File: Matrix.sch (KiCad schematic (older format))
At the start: 31 parts

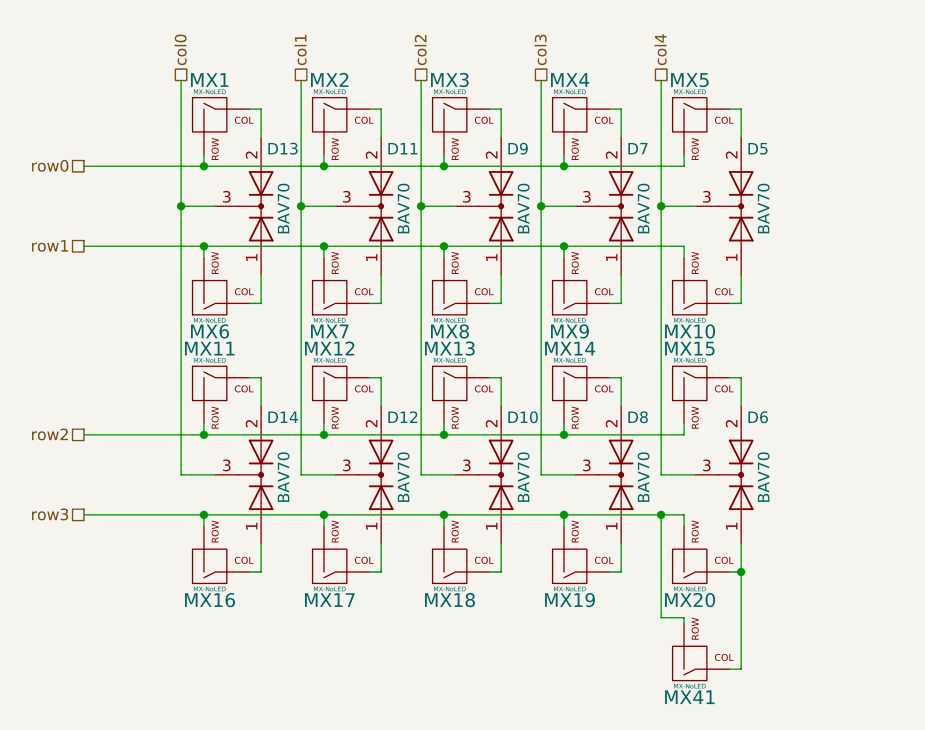
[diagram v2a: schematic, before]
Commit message: Finished right-side, added BOM
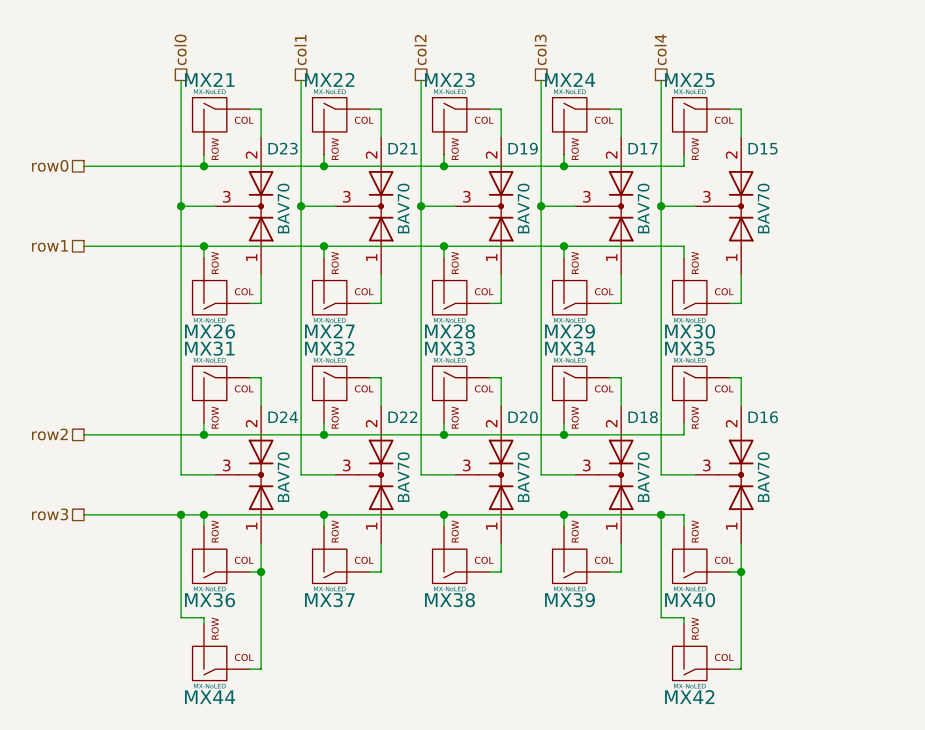
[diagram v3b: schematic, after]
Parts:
- added MX43: MX-NoLED, Ai03-MX:MXOnly-2U-Hotswap, symbol Ai03:MX-NoLED
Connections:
- net row3: now also MX43.2 (ROW)
- net at D14.1 (A), MX16.1 (COL): now also MX43.1 (COL)
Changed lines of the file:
@@
 $Descr A4 11693 8268
 encoding utf-8
-Sheet 4 5
+Sheet 5 5
 Title ""
 Date ""
@@
 AR Path="/5E0FF211/5DC40EE0" Ref="MX?"  Part="1"
 AR Path="/5E103021/5DC40EE0" Ref="MX21"  Part="1"
-F 0 "MX1" H 4725 2975 60  0000 C CNN
+F 0 "MX21" H 4725 2975 60  0000 C CNN
 F 1 "MX-NoLED" H 4725 2925 20  0000 C CNN
 F 2 "Ai03-MX:MXOnly-1U-Hotswap" H 4125 2775 60  0001 C CNN
@@
 AR Path="/5E0FF211/5DC40EF4" Ref="MX?"  Part="1"
 AR Path="/5E103021/5DC40EF4" Ref="MX26"  Part="1"
-F 0 "MX6" H 4725 3725 60  0000 C CNN
+F 0 "MX26" H 4725 3725 60  0000 C CNN
 F 1 "MX-NoLED" H 4725 3675 20  0000 C CNN
 F 2 "Ai03-MX:MXOnly-1U-Hotswap" H 4125 3525 60  0001 C CNN
@@
 AR Path="/5E0FF211/5DC4E718" Ref="MX?"  Part="1"
 AR Path="/5E103021/5DC4E718" Ref="MX31"  Part="1"
-F 0 "MX11" H 4725 4150 60  0000 C CNN
+F 0 "MX31" H 4725 4150 60  0000 C CNN
 F 1 "MX-NoLED" H 4725 4100 20  0000 C CNN
 F 2 "Ai03-MX:MXOnly-1U-Hotswap" H 4125 3950 60  0001 C CNN
@@
 AR Path="/5E0FF211/5DC4E722" Ref="D?"  Part="1"
 AR Path="/5E103021/5DC4E722" Ref="D20"  Part="1"
-F 0 "D10" V 6250 4375 50  0000 L CNN
+F 0 "D20" V 6250 4375 50  0000 L CNN
 F 1 "BAV70" H 5875 4450 50  0000 L CNN
 F 2 "Package_TO_SOT_SMD:SOT-23_Handsoldering" H 6000 4350 50  0001 C CNN
@@
 AR Path="/5E0FF211/5DC4E731" Ref="MX?"  Part="1"
 AR Path="/5E103021/5DC4E731" Ref="MX36"  Part="1"
-F 0 "MX16" H 4725 4900 60  0000 C CNN
+F 0 "MX36" H 4725 4900 60  0000 C CNN
 F 1 "MX-NoLED" H 4725 4850 20  0000 C CNN
 F 2 "Ai03-MX:MXOnly-1U-Hotswap" H 4125 4700 60  0001 C CNN
@@
 AR Path="/5E0FF211/5DC54A92" Ref="MX?"  Part="1"
 AR Path="/5E103021/5DC54A92" Ref="MX22"  Part="1"
-F 0 "MX2" H 5250 2975 60  0000 C CNN
+F 0 "MX22" H 5250 2975 60  0000 C CNN
 F 1 "MX-NoLED" H 5250 2925 20  0000 C CNN
 F 2 "Ai03-MX:MXOnly-1U-Hotswap" H 4650 2775 60  0001 C CNN
@@
 AR Path="/5E0FF211/5DC54AAB" Ref="MX?"  Part="1"
 AR Path="/5E103021/5DC54AAB" Ref="MX27"  Part="1"
-F 0 "MX7" H 5250 3725 60  0000 C CNN
+F 0 "MX27" H 5250 3725 60  0000 C CNN
 F 1 "MX-NoLED" H 5250 3675 20  0000 C CNN
 F 2 "Ai03-MX:MXOnly-1U-Hotswap" H 4650 3525 60  0001 C CNN
@@
 AR Path="/5E0FF211/5DC54AB7" Ref="MX?"  Part="1"
 AR Path="/5E103021/5DC54AB7" Ref="MX32"  Part="1"
-F 0 "MX12" H 5250 4150 60  0000 C CNN
+F 0 "MX32" H 5250 4150 60  0000 C CNN
 F 1 "MX-NoLED" H 5250 4100 20  0000 C CNN
 F 2 "Ai03-MX:MXOnly-1U-Hotswap" H 4650 3950 60  0001 C CNN
@@
 AR Path="/5E0FF211/5DC54AC1" Ref="D?"  Part="1"
 AR Path="/5E103021/5DC54AC1" Ref="D21"  Part="1"
-F 0 "D11" V 5725 3200 50  0000 L CNN
+F 0 "D21" V 5725 3200 50  0000 L CNN
 F 1 "BAV70" H 5350 3275 50  0000 L CNN
 F 2 "Package_TO_SOT_SMD:SOT-23_Handsoldering" H 5475 3175 50  0001 C CNN
@@
 AR Path="/5E0FF211/5DC54AD0" Ref="MX?"  Part="1"
 AR Path="/5E103021/5DC54AD0" Ref="MX37"  Part="1"
-F 0 "MX17" H 5250 4900 60  0000 C CNN
+F 0 "MX37" H 5250 4900 60  0000 C CNN
 F 1 "MX-NoLED" H 5250 4850 20  0000 C CNN
 F 2 "Ai03-MX:MXOnly-1U-Hotswap" H 4650 4700 60  0001 C CNN
@@
 Connection ~ 4700 3000
 Wire Wire Line
-	4700 4525 4175 4525
+	4700 4525 4600 4525
 Wire Wire Line
 	4700 4175 4175 4175
@@
 AR Path="/5E0FF211/5DC60A2A" Ref="MX?"  Part="1"
 AR Path="/5E103021/5DC60A2A" Ref="MX23"  Part="1"
-F 0 "MX3" H 5775 2975 60  0000 C CNN
+F 0 "MX23" H 5775 2975 60  0000 C CNN
 F 1 "MX-NoLED" H 5775 2925 20  0000 C CNN
 F 2 "Ai03-MX:MXOnly-1U-Hotswap" H 5175 2775 60  0001 C CNN
@@
 AR Path="/5E0FF211/5DC60A43" Ref="MX?"  Part="1"
 AR Path="/5E103021/5DC60A43" Ref="MX28"  Part="1"
-F 0 "MX8" H 5775 3725 60  0000 C CNN
+F 0 "MX28" H 5775 3725 60  0000 C CNN
 F 1 "MX-NoLED" H 5775 3675 20  0000 C CNN
 F 2 "Ai03-MX:MXOnly-1U-Hotswap" H 5175 3525 60  0001 C CNN
@@
 AR Path="/5E0FF211/5DC60A4F" Ref="MX?"  Part="1"
 AR Path="/5E103021/5DC60A4F" Ref="MX33"  Part="1"
-F 0 "MX13" H 5775 4150 60  0000 C CNN
+F 0 "MX33" H 5775 4150 60  0000 C CNN
 F 1 "MX-NoLED" H 5775 4100 20  0000 C CNN
 F 2 "Ai03-MX:MXOnly-1U-Hotswap" H 5175 3950 60  0001 C CNN
@@
 AR Path="/5E0FF211/5DC60A59" Ref="D?"  Part="1"
 AR Path="/5E103021/5DC60A59" Ref="D22"  Part="1"
-F 0 "D12" V 5725 4375 50  0000 L CNN
+F 0 "D22" V 5725 4375 50  0000 L CNN
 F 1 "BAV70" H 5350 4450 50  0000 L CNN
 F 2 "Package_TO_SOT_SMD:SOT-23_Handsoldering" H 5475 4350 50  0001 C CNN
@@
 AR Path="/5E0FF211/5DC60A68" Ref="MX?"  Part="1"
 AR Path="/5E103021/5DC60A68" Ref="MX38"  Part="1"
-F 0 "MX18" H 5775 4900 60  0000 C CNN
+F 0 "MX38" H 5775 4900 60  0000 C CNN
 F 1 "MX-NoLED" H 5775 4850 20  0000 C CNN
 F 2 "Ai03-MX:MXOnly-1U-Hotswap" H 5175 4700 60  0001 C CNN
@@
 AR Path="/5E0FF211/5DC60A77" Ref="MX?"  Part="1"
 AR Path="/5E103021/5DC60A77" Ref="MX24"  Part="1"
-F 0 "MX4" H 6300 2975 60  0000 C CNN
+F 0 "MX24" H 6300 2975 60  0000 C CNN
 F 1 "MX-NoLED" H 6300 2925 20  0000 C CNN
 F 2 "Ai03-MX:MXOnly-1U-Hotswap" H 5700 2775 60  0001 C CNN
@@
 AR Path="/5E0FF211/5DC60A90" Ref="MX?"  Part="1"
 AR Path="/5E103021/5DC60A90" Ref="MX29"  Part="1"
-F 0 "MX9" H 6300 3725 60  0000 C CNN
+F 0 "MX29" H 6300 3725 60  0000 C CNN
 F 1 "MX-NoLED" H 6300 3675 20  0000 C CNN
 F 2 "Ai03-MX:MXOnly-1U-Hotswap" H 5700 3525 60  0001 C CNN
@@
 AR Path="/5E0FF211/5DC60A9C" Ref="MX?"  Part="1"
 AR Path="/5E103021/5DC60A9C" Ref="MX34"  Part="1"
-F 0 "MX14" H 6300 4150 60  0000 C CNN
+F 0 "MX34" H 6300 4150 60  0000 C CNN
 F 1 "MX-NoLED" H 6300 4100 20  0000 C CNN
 F 2 "Ai03-MX:MXOnly-1U-Hotswap" H 5700 3950 60  0001 C CNN
@@
 AR Path="/5E0FF211/5DC60AB5" Ref="MX?"  Part="1"
 AR Path="/5E103021/5DC60AB5" Ref="MX39"  Part="1"
-F 0 "MX19" H 6300 4900 60  0000 C CNN
+F 0 "MX39" H 6300 4900 60  0000 C CNN
 F 1 "MX-NoLED" H 6300 4850 20  0000 C CNN
 F 2 "Ai03-MX:MXOnly-1U-Hotswap" H 5700 4700 60  0001 C CNN
@@
 AR Path="/5E0FF211/5DC6C6BD" Ref="MX?"  Part="1"
 AR Path="/5E103021/5DC6C6BD" Ref="MX25"  Part="1"
-F 0 "MX5" H 6825 2975 60  0000 C CNN
+F 0 "MX25" H 6825 2975 60  0000 C CNN
 F 1 "MX-NoLED" H 6825 2925 20  0000 C CNN
 F 2 "Ai03-MX:MXOnly-1U-Hotswap" H 6225 2775 60  0001 C CNN
@@
 AR Path="/5E0FF211/5DC6C6D6" Ref="MX?"  Part="1"
 AR Path="/5E103021/5DC6C6D6" Ref="MX30"  Part="1"
-F 0 "MX10" H 6825 3725 60  0000 C CNN
+F 0 "MX30" H 6825 3725 60  0000 C CNN
 F 1 "MX-NoLED" H 6825 3675 20  0000 C CNN
 F 2 "Ai03-MX:MXOnly-1U-Hotswap" H 6225 3525 60  0001 C CNN
@@
 AR Path="/5E0FF211/5DC6C6E2" Ref="MX?"  Part="1"
 AR Path="/5E103021/5DC6C6E2" Ref="MX35"  Part="1"
-F 0 "MX15" H 6825 4150 60  0000 C CNN
+F 0 "MX35" H 6825 4150 60  0000 C CNN
 F 1 "MX-NoLED" H 6825 4100 20  0000 C CNN
 F 2 "Ai03-MX:MXOnly-1U-Hotswap" H 6225 3950 60  0001 C CNN
@@
 AR Path="/5E0FF211/5DC6C6FB" Ref="MX?"  Part="1"
 AR Path="/5E103021/5DC6C6FB" Ref="MX40"  Part="1"
-F 0 "MX20" H 6825 4900 60  0000 C CNN
+F 0 "MX40" H 6825 4900 60  0000 C CNN
 F 1 "MX-NoLED" H 6825 4850 20  0000 C CNN
 F 2 "Ai03-MX:MXOnly-1U-Hotswap" H 6225 4700 60  0001 C CNN
@@
 AR Path="/5E0FF211/5E13B872" Ref="MX?"  Part="1"
 AR Path="/5E103021/5E13B872" Ref="MX42"  Part="1"
-F 0 "MX41" H 6825 5325 60  0000 C CNN
+F 0 "MX42" H 6825 5325 60  0000 C CNN
 F 1 "MX-NoLED" H 6825 5275 20  0000 C CNN
 F 2 "Ai03-MX:MXOnly-2U-Hotswap" H 6225 5125 60  0001 C CNN
@@
 AR Path="/5E0FF211/5DC60AA6" Ref="D?"  Part="1"
 AR Path="/5E103021/5DC60AA6" Ref="D23"  Part="1"
-F 0 "D13" V 5200 3200 50  0000 L CNN
+F 0 "D23" V 5200 3200 50  0000 L CNN
 F 1 "BAV70" H 4825 3275 50  0000 L CNN
 F 2 "Package_TO_SOT_SMD:SOT-23_Handsoldering" H 4950 3175 50  0001 C CNN
@@
 AR Path="/5E0FF211/5DC60A34" Ref="D?"  Part="1"
 AR Path="/5E103021/5DC60A34" Ref="D17"  Part="1"
-F 0 "D7" V 6775 3200 50  0000 L CNN
+F 0 "D17" V 6775 3200 50  0000 L CNN
 F 1 "BAV70" H 6400 3275 50  0000 L CNN
 F 2 "Package_TO_SOT_SMD:SOT-23_Handsoldering" H 6525 3175 50  0001 C CNN
@@
 AR Path="/5E0FF211/5DC60A81" Ref="D?"  Part="1"
 AR Path="/5E103021/5DC60A81" Ref="D18"  Part="1"
-F 0 "D8" V 6775 4375 50  0000 L CNN
+F 0 "D18" V 6775 4375 50  0000 L CNN
 F 1 "BAV70" H 6400 4450 50  0000 L CNN
 F 2 "Package_TO_SOT_SMD:SOT-23_Handsoldering" H 6525 4350 50  0001 C CNN
@@
 AR Path="/5E0FF211/5DC6C6EC" Ref="D?"  Part="1"
 AR Path="/5E103021/5DC6C6EC" Ref="D24"  Part="1"
-F 0 "D14" V 5200 4375 50  0000 L CNN
+F 0 "D24" V 5200 4375 50  0000 L CNN
 F 1 "BAV70" H 4825 4450 50  0000 L CNN
 F 2 "Package_TO_SOT_SMD:SOT-23_Handsoldering" H 4950 4350 50  0001 C CNN
@@
 AR Path="/5E0FF211/5DC54A9C" Ref="D?"  Part="1"
 AR Path="/5E103021/5DC54A9C" Ref="D16"  Part="1"
-F 0 "D6" V 7300 4375 50  0000 L CNN
+F 0 "D16" V 7300 4375 50  0000 L CNN
 F 1 "BAV70" H 6925 4450 50  0000 L CNN
 F 2 "Package_TO_SOT_SMD:SOT-23_Handsoldering" H 7050 4350 50  0001 C CNN
@@
 AR Path="/5E0FF211/5DC6C6C7" Ref="D?"  Part="1"
 AR Path="/5E103021/5DC6C6C7" Ref="D19"  Part="1"
-F 0 "D9" V 6250 3200 50  0000 L CNN
+F 0 "D19" V 6250 3200 50  0000 L CNN
 F 1 "BAV70" H 5875 3275 50  0000 L CNN
 F 2 "Package_TO_SOT_SMD:SOT-23_Handsoldering" H 6000 3175 50  0001 C CNN
@@
 AR Path="/5E0FF211/5DC40EEA" Ref="D?"  Part="1"
 AR Path="/5E103021/5DC40EEA" Ref="D15"  Part="1"
-F 0 "D5" V 7300 3200 50  0000 L CNN
+F 0 "D15" V 7300 3200 50  0000 L CNN
 F 1 "BAV70" H 6925 3275 50  0000 L CNN
 F 2 "Package_TO_SOT_SMD:SOT-23_Handsoldering" H 7050 3175 50  0001 C CNN
@@
 	0    1    -1   0
 $EndComp
+$Comp
+L Ai03:MX-NoLED MX?
+U 1 1 5DCDB48C
+P 4750 5150
+AR Path="/5DCDB48C" Ref="MX?"  Part="1"
+AR Path="/5DBF64D6/5DCDB48C" Ref="MX43"  Part="1"
+AR Path="/5E0FF211/5DCDB48C" Ref="MX?"  Part="1"
+AR Path="/5E103021/5DCDB48C" Ref="MX44"  Part="1"
+F 0 "MX44" H 4725 5325 60  0000 C CNN
+F 1 "MX-NoLED" H 4725 5275 20  0000 C CNN
+F 2 "Ai03-MX:MXOnly-2U-Hotswap" H 4125 5125 60  0001 C CNN
+F 3 "" H 4125 5125 60  0001 C CNN
+	1    4750 5150
+	1    0    0    1
+$EndComp
+Wire Wire Line
+	4700 4975 4600 4975
+Wire Wire Line
+	4600 4975 4600 4525
+Connection ~ 4600 4525
+Wire Wire Line
+	4600 4525 4175 4525
+Wire Wire Line
+	4700 4975 4700 5000
+Wire Wire Line
+	4900 5200 4950 5200
+Wire Wire Line
+	4950 5200 4950 4775
+Connection ~ 4950 4775
 $EndSCHEMATC

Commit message: Started work on adding extra col
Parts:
- removed MX18: MX-NoLED, Ai03-MX:MXOnly-1U-Hotswap, symbol Ai03:MX-NoLED
- removed MX43: MX-NoLED, Ai03-MX:MXOnly-2U-Hotswap, symbol Ai03:MX-NoLED
- added D5, D6: BAV70, Package_TO_SOT_SMD:SOT-23_Handsoldering, symbol Device:D_x2_KCom_AAK
- added MX12, MX21, MX22, MX23, MXA24: MX-NoLED, Ai03-MX:MXOnly-1U-Hotswap, symbol Ai03:MX-NoLED
- added MXB19: MX-NoLED, Ai03-MX:MXOnly-2U-Hotswap, symbol Ai03:MX-NoLED
- renumbered D5 to D3, D6 to D4, MX12 to MX18, MX19 to MXA19, MX41 to MXB24
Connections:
- net col4: now also D5.3 (K), D6.3 (K); no longer D3.3 (K), D4.3 (K)
- net row0: now also MX6.2 (ROW)
- net row1: now also MX11.2 (ROW), MX12.2 (ROW); no longer MX6.2 (ROW)
- net row2: now also MX16.2 (ROW), MX17.2 (ROW); no longer MX11.2 (ROW)
- net row3: now also MX21.2 (ROW), MX22.2 (ROW), MX23.2 (ROW), MXA24.2 (ROW), MXB19.2 (ROW); no longer MX16.2 (ROW), MX17.2 (ROW)
- net at D3.1 (A): now also MX12.1 (COL); no longer MX10.1 (COL)
- net at D3.2 (A): now also MX6.1 (COL); no longer MX5.1 (COL)
- net at D13.1 (A): now also MX7.1 (COL); no longer MX6.1 (COL)
- net at MX11.1 (COL): now also D5.1 (A); no longer D14.2 (A)
- net at D10.1 (A): now also MX21.1 (COL)
- net at D10.2 (A): now also MX15.1 (COL); no longer MX13.1 (COL)
- net at MX16.1 (COL): now also D8.2 (A); no longer D14.1 (A)
- net at D4.1 (A), MXB24.1 (COL): now also MXA24.1 (COL); no longer MX20.1 (COL)
- net at D4.2 (A): now also MX18.1 (COL); no longer MX15.1 (COL)
- net at D11.1 (A): now also MX8.1 (COL); no longer MX7.1 (COL)
- net at D12.2 (A): now also MX14.1 (COL); no longer MX18.1 (COL)
- net at D12.1 (A): now also MX20.1 (COL); no longer MX17.1 (COL)
- net at D7.1 (A): now also MX10.1 (COL); no longer MX9.1 (COL)
- net at D9.1 (A): now also MX9.1 (COL); no longer MX8.1 (COL)
- net at D8.1 (A): now also MX22.1 (COL); no longer MXA19.1 (COL)
- new net: D14.2 (A), MX13.1 (COL)
- new net: D14.1 (A), MXA19.1 (COL), MXB19.1 (COL)
- new net: D5.2 (A), MX5.1 (COL)
- new net: D6.2 (A), MX17.1 (COL)
- new net: D6.1 (A), MX23.1 (COL)
- new net col5: D3.3 (K), D4.3 (K)
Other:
- moved on the sheet: D15, D16, MX30, MX31, MX32, MX33, MX34, MX35, MX37, MX38, MX39, MX40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
